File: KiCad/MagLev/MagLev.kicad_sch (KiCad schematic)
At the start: 50 parts, among them J1 Barrel_Jack, Q11 Q_NMOS_DGS, Q12 Q_NMOS_DGS, Q13 Q_NMOS_DGS, Q15 Q_NMOS_DGS, Q5 ZX5T1951GTA, U10 DRV5505, U11 DRV5505, U12 DRV5505, U13 MCP1402, U14 MCP1402, U15 MCP1402, U3 L78L05_SO8, U4 TL431A, U5 LM393, U7 MCP1402, X1 L_Ferrite, X2 L_Ferrite, Y1 L_Ferrite, Y2 L_Ferrite, Y4 L_Ferrite, Y5 L_Ferrite, Y6 L_Ferrite, Y7 L_Ferrite

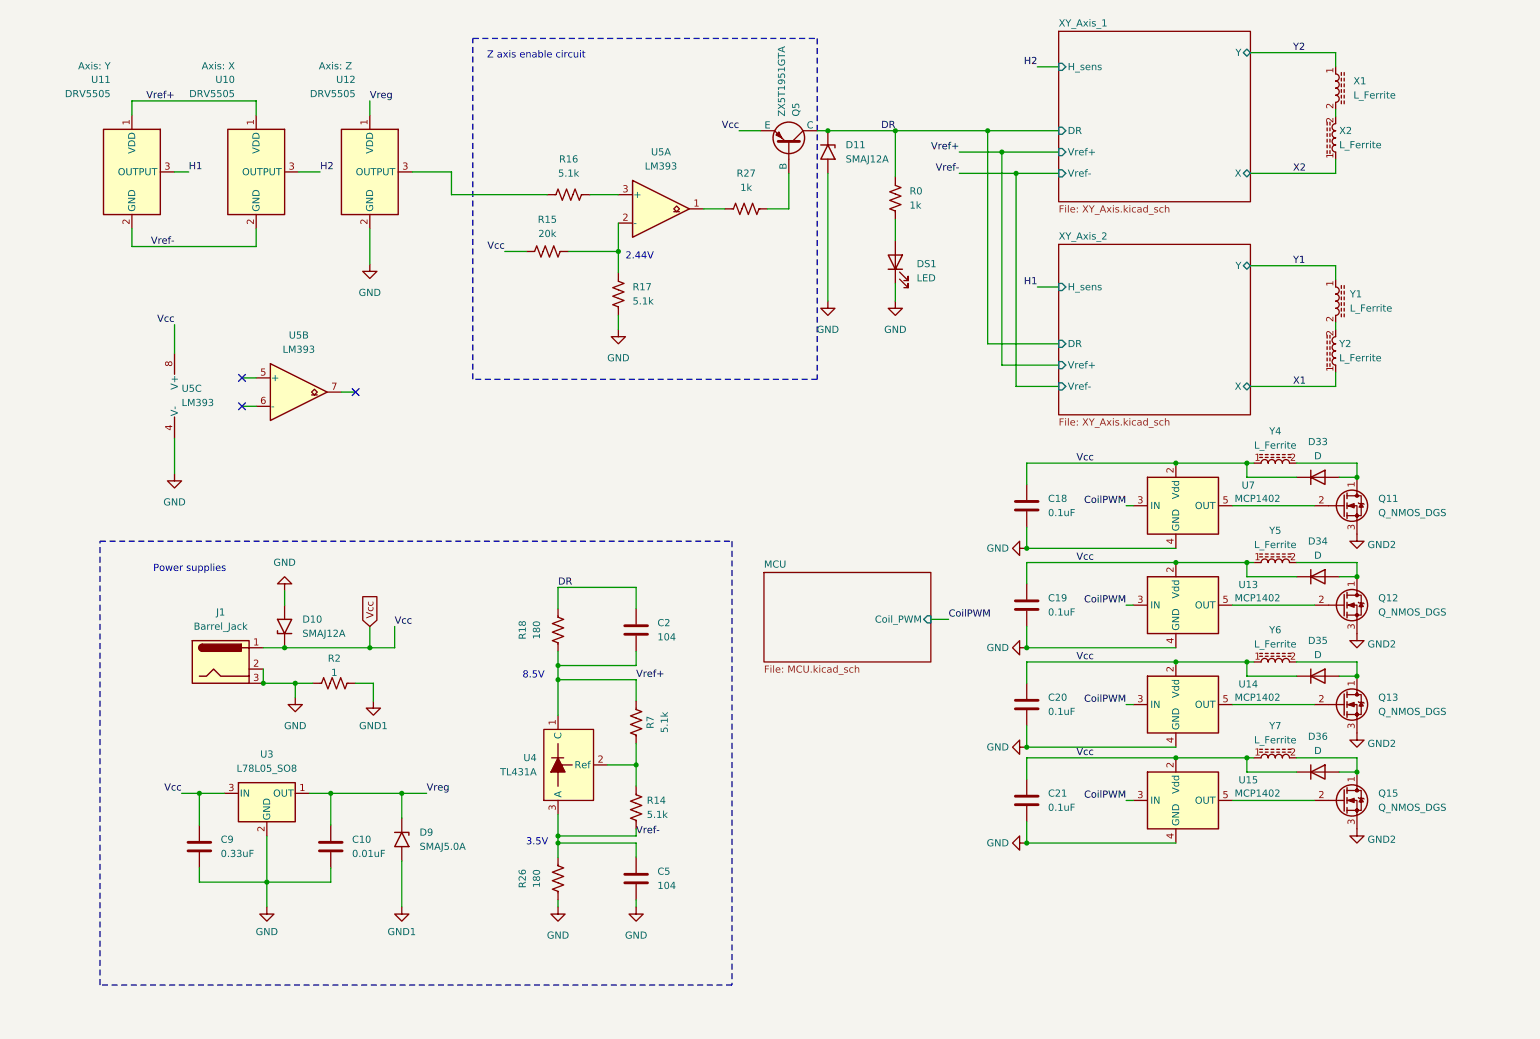
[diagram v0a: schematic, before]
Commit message: Add MCU enable circuit and leds.
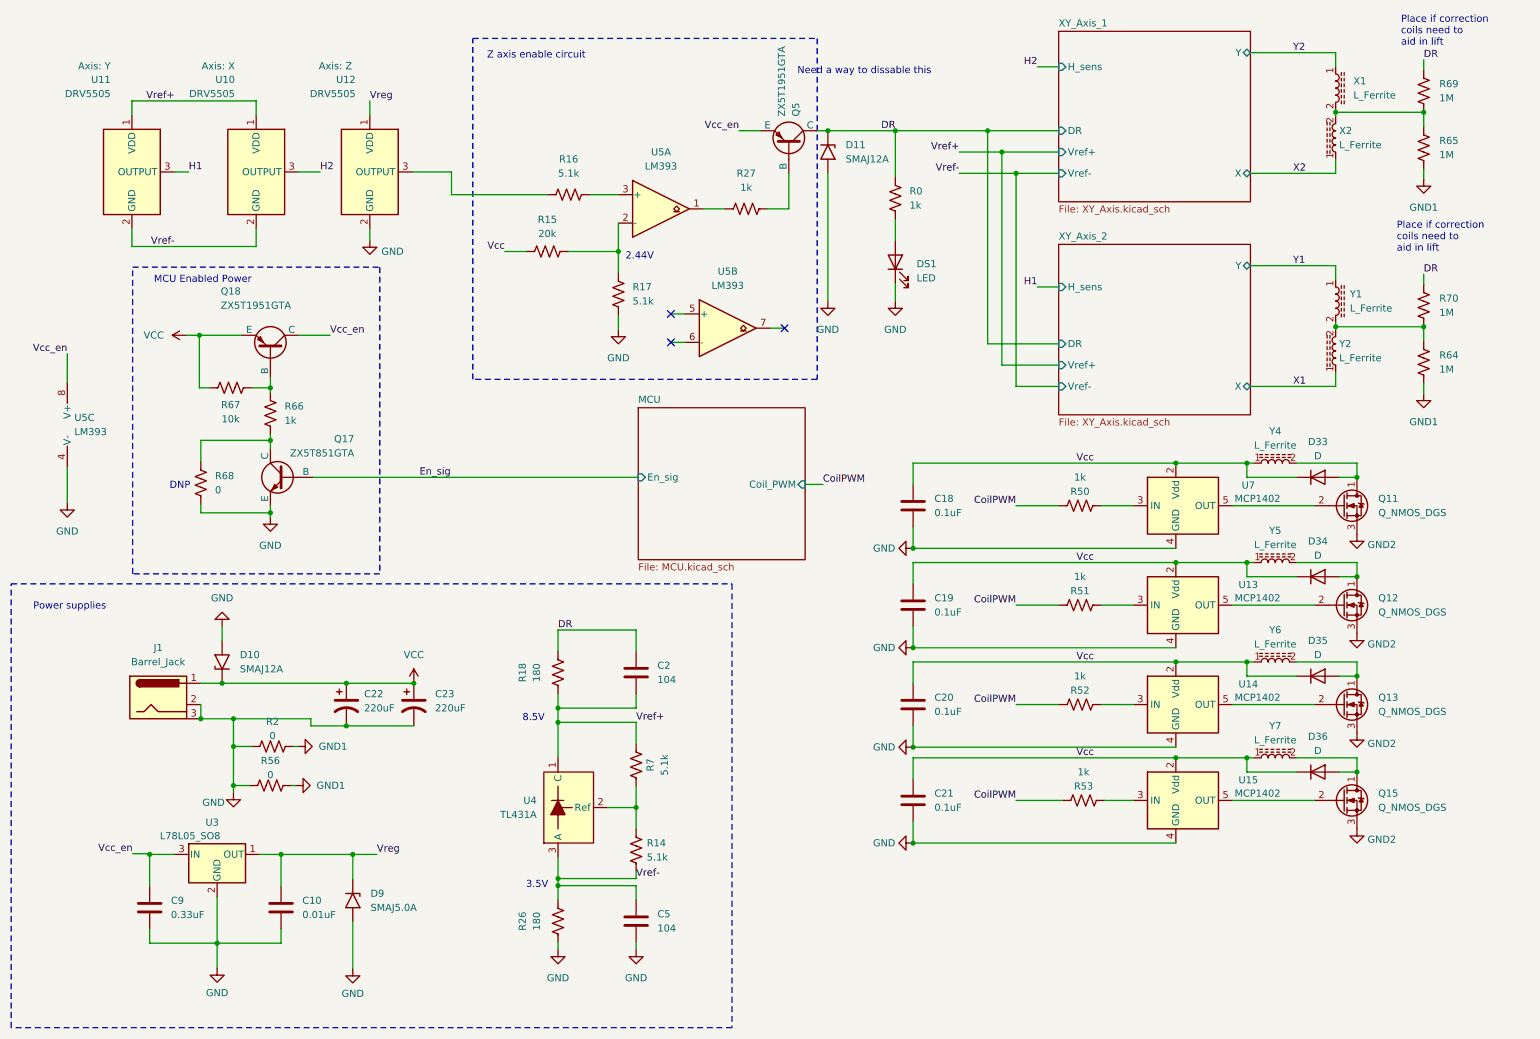
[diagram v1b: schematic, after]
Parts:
- added C22, C23: 220uF, Capacitor_SMD:CP_Elec_8x10, symbol Device:C_Polarized_US
- added Q17: ZX5T851GTA, Maglev_Footprint_Library:SOT-223-3_TabPin2_BJT, symbol Simulation_SPICE:NPN
- added Q18: ZX5T1951GTA, Maglev_Footprint_Library:SOT-223-3_TabPin2_BJT, symbol Simulation_SPICE:PNP
- added R50, R51, R52, R53, R66: 1k, Resistor_SMD:R_0805_2012Metric_Pad1.20x1.40mm_HandSolder, symbol Device:R_US
- added R56: 0, symbol Device:R_US
- added R64, R65, R69, R70: 1M, symbol Device:R_US
- added R67: 10k, Resistor_SMD:R_0805_2012Metric_Pad1.20x1.40mm_HandSolder, symbol Device:R_US
- added R68: 0, Resistor_SMD:R_0805_2012Metric_Pad1.20x1.40mm_HandSolder, symbol Device:R_US
- R2: value 1 -> 0; footprint Resistor_SMD:R_0805_2012Metric_Pad1.20x1.40mm_HandSolder -> (none)
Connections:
- net CoilPWM: now also R50.2, R51.2, R52.2, R53.2; no longer U13.3 (IN), U14.3 (IN), U15.3 (IN), U7.3 (IN)
- net DR: now also R69.1, R70.1
- net GND: now also D9.2 (A2), C22.2, C23.2, Q17.3 (E), R56.1, R68.2
- net GND1: now also R56.2, R64.2, R65.2; no longer D9.2 (A2)
- net Vcc: no longer C9.1, D10.1 (A1), J1.1, Q5.3 (E), U3.3 (IN), U5.8 (V+)
- net at X1.2, X2.2: now also R65.1, R69.2
- net at Y1.2, Y2.2: now also R64.1, R70.2
- new net: R53.1, U15.3 (IN)
- new net: R50.1, U7.3 (IN)
- new net: Q18.2 (B), R66.1, R67.1
- new net: R51.1, U13.3 (IN)
- new net: Q17.1 (C), R66.2, R68.1
- new net: R52.1, U14.3 (IN)
- new net En_sig: Q17.2 (B)
- new net VCC: C22.1, C23.1, D10.1 (A1), J1.1, Q18.3 (E), R67.2
- new net Vcc_en: C9.1, Q18.1 (C), Q5.3 (E), U3.3 (IN), U5.8 (V+)
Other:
- sheet MCU ports: added En_sig; removed none
- note added: "DNP"
- note added: "MCU Enabled Power"
- note added: "Need a way to dissable this"
- note added: "Place if correction coils need to aid in lift"
- moved on the sheet: C10, C18, C19, C2, C20, C21, C5, C9, D10, D9, J1, R14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

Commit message: Assign footprints to MCU components.
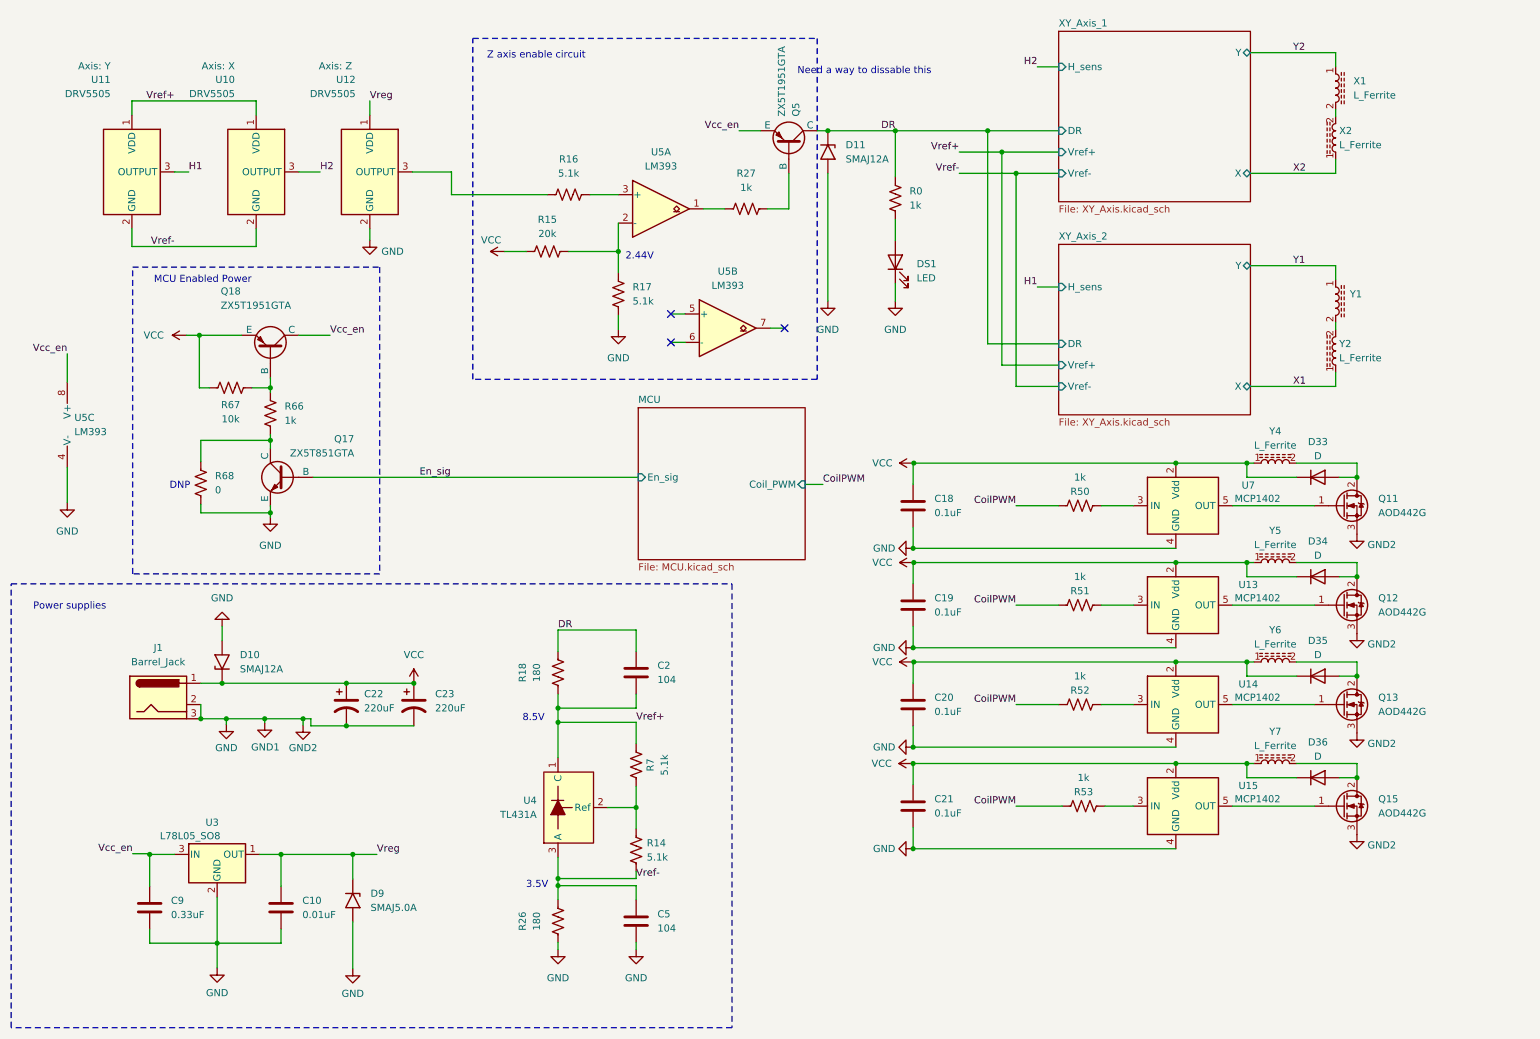
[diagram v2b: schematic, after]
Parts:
- removed Q11, Q12, Q13, Q15: Q_NMOS_DGS, symbol Device:Q_NMOS_DGS
- removed R2, R56: 0, symbol Device:R_US
- removed R64, R65, R69, R70: 1M, symbol Device:R_US
- added Q11, Q12, Q13, Q15: AOD442G, Package_TO_SOT_SMD:TO-252-2, symbol Device:Q_NMOS_GDS
- C22, C23: footprint Capacitor_SMD:CP_Elec_8x10 -> Maglev_Footprint_Library:CP_Elec_8x10_HandSolder
- D33, D34, D35, D36: footprint (none) -> Maglev_Footprint_Library:TO-252-Schottkey
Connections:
- net Vcc is gone; now on net VCC: C18.1, C19.1, C20.1, C21.1, D33.1 (K), D34.1 (K), D35.1 (K), D36.1 (K), R15.1, U13.2 (Vdd), U14.2 (Vdd), U15.2 (Vdd), U7.2 (Vdd), Y4.1, Y5.1, Y6.1, Y7.1
- net GND: now also Q11.3 (S), Q12.3 (S), Q13.3 (S), Q15.3 (S)
- net at D34.2 (A), Y5.2: now also Q12.2 (D)
- net at U13.5 (OUT): now also Q12.1 (G)
- net at D36.2 (A), Y7.2: now also Q15.2 (D)
- net at U15.5 (OUT): now also Q15.1 (G)
- net at U7.5 (OUT): now also Q11.1 (G)
- net at D35.2 (A), Y6.2: now also Q13.2 (D)
- net at U14.5 (OUT): now also Q13.1 (G)
- net at D33.2 (A), Y4.2: now also Q11.2 (D)
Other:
- note removed: "Place if correction coils need to aid in lift"
- moved on the sheet: C21, D36, R53, U15, Y7

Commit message: Series coils, add TPs.
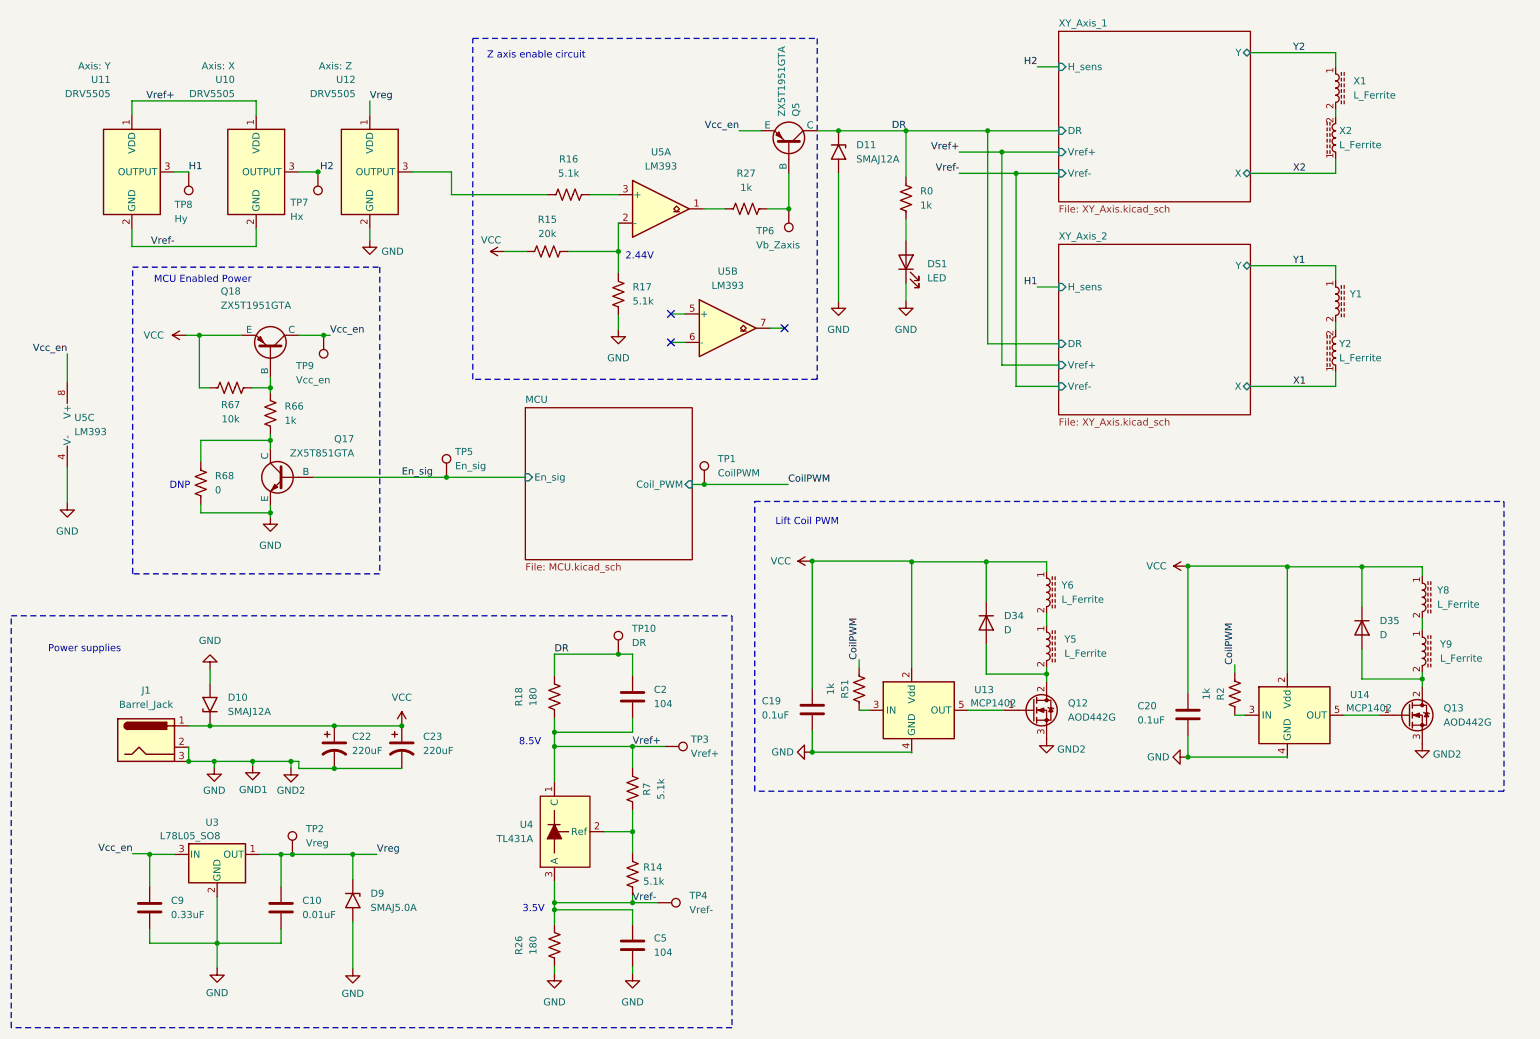
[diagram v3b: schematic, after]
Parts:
- removed C18, C21: 0.1uF, Capacitor_SMD:C_0805_2012Metric_Pad1.18x1.45mm_HandSolder, symbol Device:C
- removed D33, D36: D, Maglev_Footprint_Library:TO-252-Schottkey, symbol Device:D
- removed Q11, Q15: AOD442G, Package_TO_SOT_SMD:TO-252-2, symbol Device:Q_NMOS_GDS
- removed R50, R52, R53: 1k, Resistor_SMD:R_0805_2012Metric_Pad1.20x1.40mm_HandSolder, symbol Device:R_US
- removed U15, U7: MCP1402, Package_TO_SOT_SMD:SOT-23-5, symbol Driver_FET:MCP1416
- removed Y4, Y7: L_Ferrite, Maglev_Footprint_Library:Maglev_coil, symbol Device:L_Ferrite
- added R2: 1k, Resistor_SMD:R_0805_2012Metric_Pad1.20x1.40mm_HandSolder, symbol Device:R_US
- added TP1: CoilPWM, TestPoint:TestPoint_Pad_D2.0mm, symbol Connector:TestPoint
- added TP10: DR, TestPoint:TestPoint_Pad_D2.0mm, symbol Connector:TestPoint
- added TP2: Vreg, TestPoint:TestPoint_Pad_D2.0mm, symbol Connector:TestPoint
- added TP3: Vref+, TestPoint:TestPoint_Pad_D2.0mm, symbol Connector:TestPoint
- added TP4: Vref-, TestPoint:TestPoint_Pad_D2.0mm, symbol Connector:TestPoint
- added TP5: En_sig, TestPoint:TestPoint_Pad_D2.0mm, symbol Connector:TestPoint
- added TP6: Vb_Zaxis, TestPoint:TestPoint_Pad_D2.0mm, symbol Connector:TestPoint
- added TP7: Hx, TestPoint:TestPoint_Pad_D2.0mm, symbol Connector:TestPoint
- added TP8: Hy, TestPoint:TestPoint_Pad_D2.0mm, symbol Connector:TestPoint
- added TP9: Vcc_en, TestPoint:TestPoint_Pad_D2.0mm, symbol Connector:TestPoint
- added Y8, Y9: L_Ferrite, Maglev_Footprint_Library:Maglev_coil, symbol Device:L_Ferrite
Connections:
- net CoilPWM: now also R51.1, R2.1, TP1.1; no longer R51.2
- net DR: now also TP10.1
- net En_sig: now also TP5.1
- net H1: now also TP8.1
- net H2: now also TP7.1
- net VCC: now also Y8.1; no longer Y5.1
- net Vcc_en: now also TP9.1
- net Vref+: now also TP3.1
- net Vref-: now also TP4.1
- net Vreg: now also TP2.1
- net at Q5.2 (B), R27.2: now also TP6.1
- net at U13.3 (IN): now also R51.2; no longer R51.1
- net at D35.2 (A), Q13.2 (D): now also Y9.2; no longer Y6.2
- net at U14.3 (IN): now also R2.2
- new net: Y8.2, Y9.1
- new net: Y5.1, Y6.2
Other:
- note added: "Lift Coil PWM"
- note removed: "Need a way to dissable this"
- moved on the sheet: C19, C2, C22, C23, C5, D10, D11, D34, DS1, J1, Q12, R0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
